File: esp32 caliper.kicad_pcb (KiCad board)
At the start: 2 copper layers, 58 x 38.3 mm, 44 parts, among them J1 USB4105-GF-A, J2 Current Testing, Q1 BC846BLT1G, Q2 BC846BLT1G, Q3 SSM3K36FS, SW1 Boot, SW2 Rst, SW3 SendEnter, SW4 SendSpace, U1 MCP73831T-5ACI/OT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

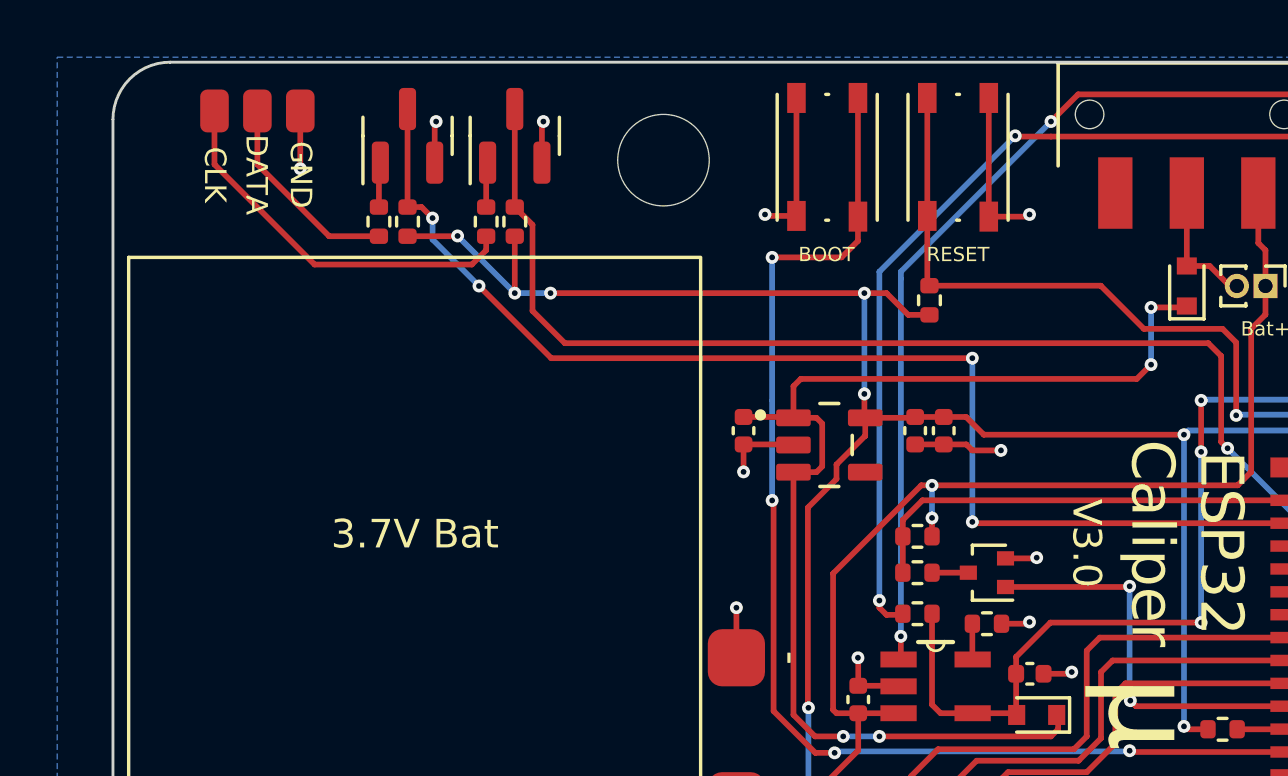
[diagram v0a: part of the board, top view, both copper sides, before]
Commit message: add 1.5v output
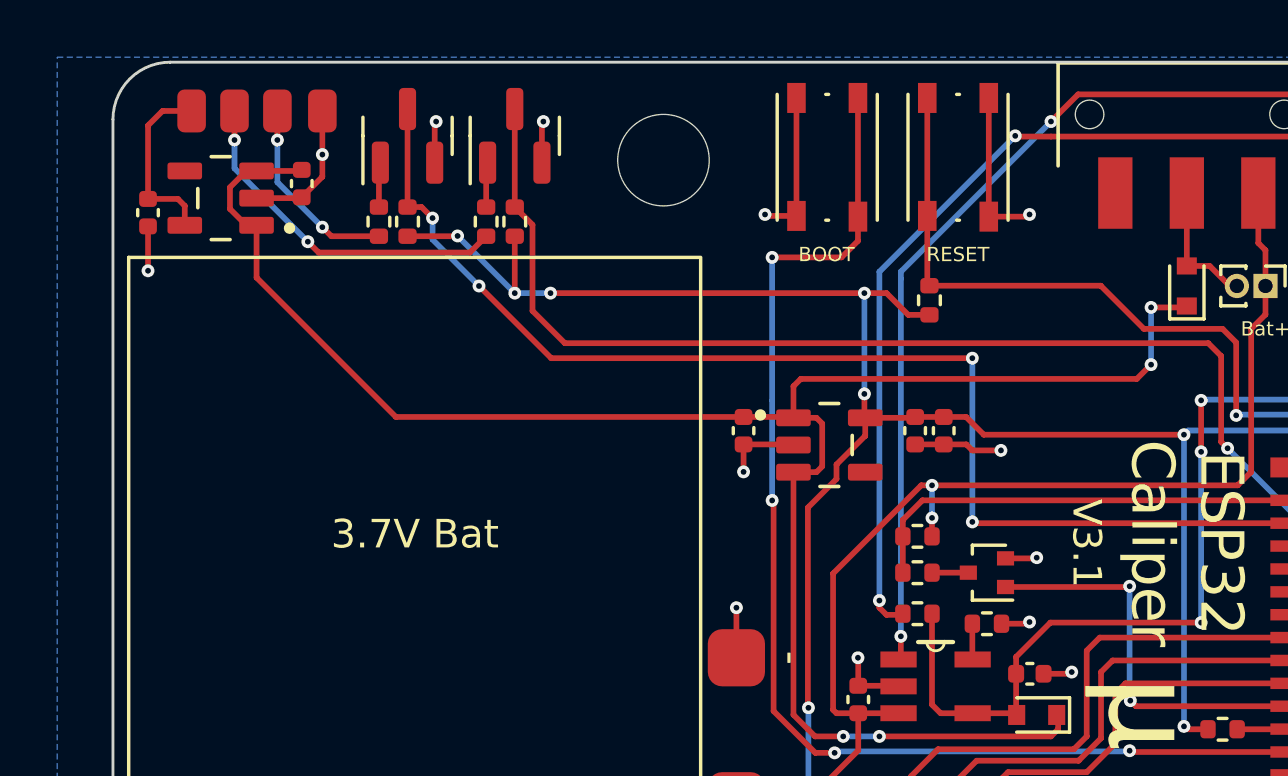
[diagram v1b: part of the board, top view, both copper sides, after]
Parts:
- added C6: 1u, Capacitor_SMD:C_0402_1005Metric, F.Cu at (143.6, 58.4)
- added C7: 1u, Capacitor_SMD:C_0402_1005Metric, F.Cu at (138.2, 59.4)
- added U5: LP5907MFX-1.5/NOPB, 1V5Reg:SOT95P280X145-5N, F.Cu at (140.7, 58.9)
- moved U2 0.80 mm to (139.7, 55.9)
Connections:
- U2 pad 1: /CLKIN -> +1V5
- U2 pad 2: /DATAIN -> /CLKIN
- U2 pad 3: GND -> /DATAIN
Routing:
- net VDD: track 41.3 -> 66.9 mm
- net +1V5: track 0.00 -> 6.37 mm
- net GND: track 137.6 -> 142.1 mm, vias 21 -> 22
- net /CLKIN: track 13.5 -> 11.8 mm, vias 0 -> 2
- net /DATAIN: track 7.16 -> 6.82 mm, vias 0 -> 2
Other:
- board text added: "V3.1"
- board text removed: "CLK"
- board text removed: "DATA"
- board text removed: "V3.0"
